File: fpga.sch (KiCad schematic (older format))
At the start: 1 part

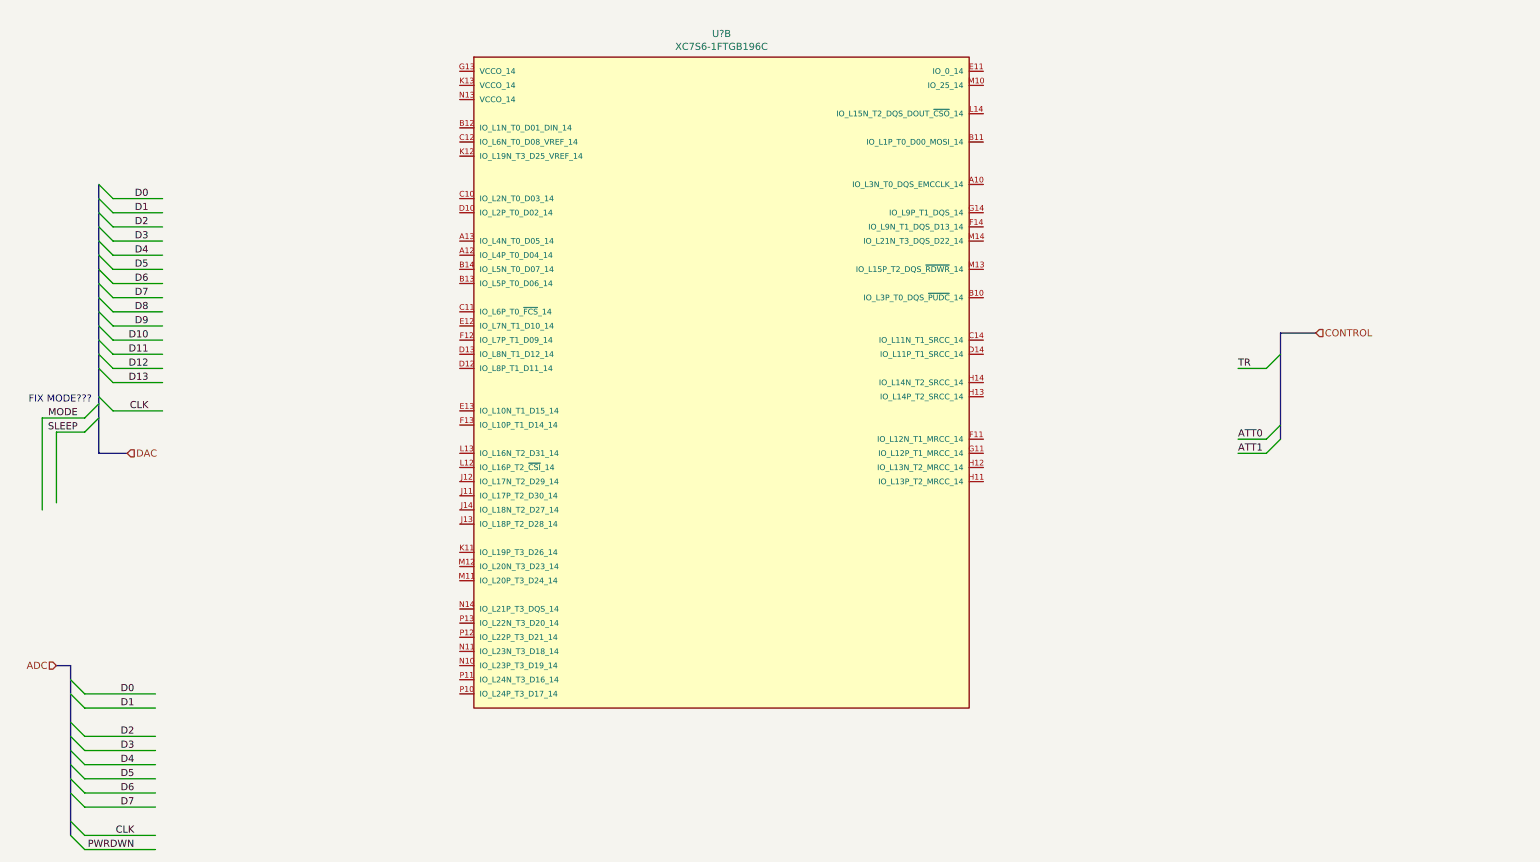
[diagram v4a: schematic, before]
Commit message: Begin the implementation of Human in-out, a few small changes
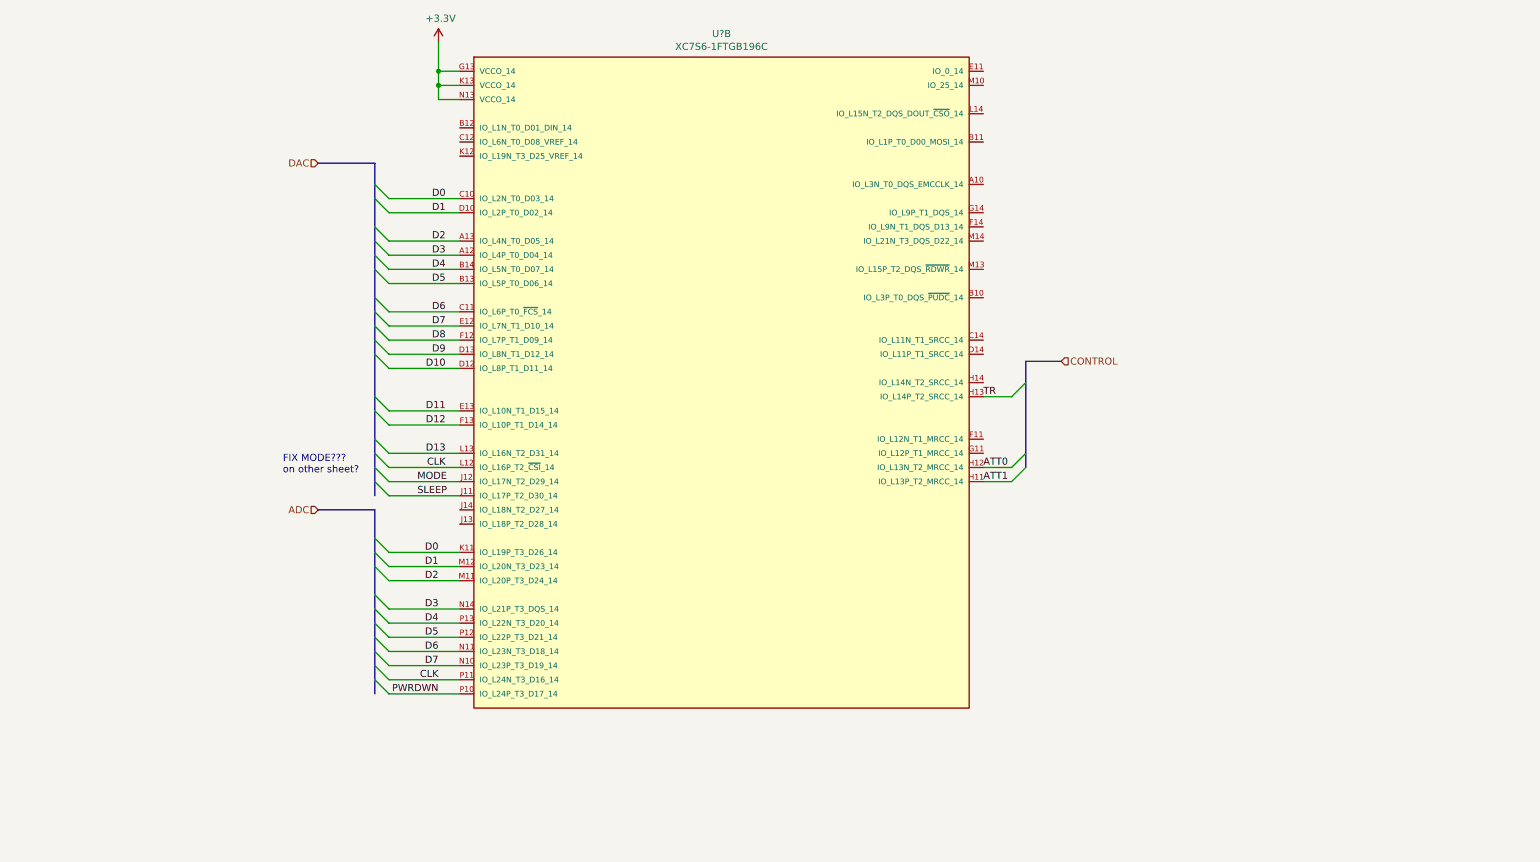
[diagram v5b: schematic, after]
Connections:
- net labels added: +3.3V
- wire segments 32 -> 36
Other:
- note added: "FIX MODE???\non other sheet?"
- note removed: "FIX MODE???"
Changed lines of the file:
@@
 $Descr A4 11693 8268
 encoding utf-8
-Sheet 11 16
+Sheet 11 17
 Title "Open HF SDR FPGA Sheet"
 Date "2021-01-16"
@@
 	1    0    0    -1
 $EndComp
-Text HLabel 1400 5800 0    50   Input ~ 0
+Text HLabel 3250 4700 0    50   Input ~ 0
 ADC
 Entry Wire Line
-	1500 5900 1600 6000
-Entry Wire Line
-	1600 6100 1500 6000
-Entry Wire Line
-	1600 6300 1500 6200
-Entry Wire Line
-	1600 6400 1500 6300
-Entry Wire Line
-	1600 6500 1500 6400
-Entry Wire Line
-	1600 6600 1500 6500
-Entry Wire Line
-	1600 6700 1500 6600
-Entry Wire Line
-	1600 6800 1500 6700
-Entry Wire Line
-	1600 7000 1500 6900
-Entry Wire Line
-	1600 7100 1500 7000
-Wire Wire Line
-	2100 6000 1600 6000
-Wire Wire Line
-	2100 6100 1600 6100
-Wire Wire Line
-	1600 6300 2100 6300
-Wire Wire Line
-	2100 6400 1600 6400
-Wire Wire Line
-	2100 6500 1600 6500
-Wire Wire Line
-	2100 6600 1600 6600
-Wire Wire Line
-	2100 6700 1600 6700
-Wire Wire Line
-	2100 6800 1600 6800
-Wire Wire Line
-	2100 7000 1600 7000
-Wire Wire Line
-	2100 7100 1600 7100
-Text Label 1950 6000 2    50   ~ 0
+	3650 4900 3750 5000
+Entry Wire Line
+	3750 5100 3650 5000
+Entry Wire Line
+	3750 5200 3650 5100
+Entry Wire Line
+	3750 5400 3650 5300
+Entry Wire Line
+	3750 5500 3650 5400
+Entry Wire Line
+	3750 5600 3650 5500
+Entry Wire Line
+	3750 5700 3650 5600
+Entry Wire Line
+	3750 5800 3650 5700
+Entry Wire Line
+	3750 5900 3650 5800
+Entry Wire Line
+	3750 6000 3650 5900
+Wire Wire Line
+	4250 5000 3750 5000
+Wire Wire Line
+	4250 5100 3750 5100
+Wire Wire Line
+	3750 5200 4250 5200
+Wire Wire Line
+	4250 5400 3750 5400
+Wire Wire Line
+	4250 5500 3750 5500
+Wire Wire Line
+	4250 5600 3750 5600
+Wire Wire Line
+	4250 5700 3750 5700
+Wire Wire Line
+	4250 5800 3750 5800
+Wire Wire Line
+	4250 5900 3750 5900
+Wire Wire Line
+	4250 6000 3750 6000
+Text Label 4100 5000 2    50   ~ 0
 D0
-Text Label 1950 6100 2    50   ~ 0
+Text Label 4100 5100 2    50   ~ 0
 D1
-Text Label 1950 6300 2    50   ~ 0
+Text Label 4100 5200 2    50   ~ 0
 D2
-Text Label 1950 6400 2    50   ~ 0
+Text Label 4100 5400 2    50   ~ 0
 D3
-Text Label 1950 6500 2    50   ~ 0
+Text Label 4100 5500 2    50   ~ 0
 D4
-Text Label 1950 6600 2    50   ~ 0
+Text Label 4100 5600 2    50   ~ 0
 D5
-Text Label 1950 6700 2    50   ~ 0
+Text Label 4100 5700 2    50   ~ 0
 D6
-Text Label 1950 6800 2    50   ~ 0
+Text Label 4100 5800 2    50   ~ 0
 D7
-Text Label 1950 7000 2    50   ~ 0
+Text Label 4100 5900 2    50   ~ 0
 CLK
-Text Label 1950 7100 2    50   ~ 0
+Text Label 4100 6000 2    50   ~ 0
 PWRDWN
-Wire Bus Line
-	1500 5800 1400 5800
-Entry Wire Line
-	1800 2500 1700 2400
-Entry Wire Line
-	1800 2600 1700 2500
-Entry Wire Line
-	1800 2700 1700 2600
-Entry Wire Line
-	1800 2800 1700 2700
-Entry Wire Line
-	1800 2900 1700 2800
-Entry Wire Line
-	1800 3000 1700 2900
-Entry Wire Line
-	1800 3100 1700 3000
-Entry Wire Line
-	1800 3200 1700 3100
-Entry Wire Line
-	1800 3300 1700 3200
-Entry Wire Line
-	1800 3400 1700 3300
-Entry Wire Line
-	1800 3500 1700 3400
-Entry Wire Line
-	1800 3600 1700 3500
-Entry Wire Line
-	1800 3700 1700 3600
-Entry Wire Line
-	1800 3800 1700 3700
-Entry Wire Line
-	1800 4000 1700 3900
-Wire Wire Line
-	2150 2500 1800 2500
-Wire Wire Line
-	2150 2600 1800 2600
-Wire Wire Line
-	2150 2700 1800 2700
-Wire Wire Line
-	2150 2800 1800 2800
-Wire Wire Line
-	2150 2900 1800 2900
-Wire Wire Line
-	2150 3000 1800 3000
-Wire Wire Line
-	2150 3100 1800 3100
-Wire Wire Line
-	2150 3200 1800 3200
-Wire Wire Line
-	2150 3300 1800 3300
-Wire Wire Line
-	2150 3400 1800 3400
-Wire Wire Line
-	2150 3500 1800 3500
-Wire Wire Line
-	2150 3600 1800 3600
-Wire Wire Line
-	2150 3700 1800 3700
-Wire Wire Line
-	2150 3800 1800 3800
-Wire Wire Line
-	2150 4000 1800 4000
-Text Label 2050 2500 2    50   ~ 0
+Entry Wire Line
+	3750 2500 3650 2400
+Entry Wire Line
+	3750 2600 3650 2500
+Entry Wire Line
+	3750 2800 3650 2700
+Entry Wire Line
+	3750 2900 3650 2800
+Entry Wire Line
+	3750 3000 3650 2900
+Entry Wire Line
+	3750 3100 3650 3000
+Entry Wire Line
+	3750 3300 3650 3200
+Entry Wire Line
+	3750 3400 3650 3300
+Entry Wire Line
+	3750 3500 3650 3400
+Entry Wire Line
+	3750 3600 3650 3500
+Entry Wire Line
+	3750 3700 3650 3600
+Entry Wire Line
+	3750 4000 3650 3900
+Entry Wire Line
+	3750 4100 3650 4000
+Entry Wire Line
+	3750 4300 3650 4200
+Entry Wire Line
+	3750 4400 3650 4300
+Wire Wire Line
+	4250 2500 3750 2500
+Wire Wire Line
+	4250 2600 3750 2600
+Wire Wire Line
+	4250 2800 3750 2800
+Wire Wire Line
+	4250 2900 3750 2900
+Wire Wire Line
+	4250 3000 3750 3000
+Wire Wire Line
+	4250 3100 3750 3100
+Wire Wire Line
+	4250 3300 3750 3300
+Wire Wire Line
+	4250 3400 3750 3400
+Wire Wire Line
+	4250 3500 3750 3500
+Wire Wire Line
+	4250 3600 3750 3600
+Wire Wire Line
+	4250 3700 3750 3700
+Wire Wire Line
+	4250 4000 3750 4000
+Wire Wire Line
+	4250 4100 3750 4100
+Wire Wire Line
+	4250 4300 3750 4300
+Wire Wire Line
+	4250 4400 3750 4400
+Text Label 4150 2500 2    50   ~ 0
 D0
-Text Label 2050 2600 2    50   ~ 0
+Text Label 4150 2600 2    50   ~ 0
 D1
-Text Label 2050 2700 2    50   ~ 0
+Text Label 4150 2800 2    50   ~ 0
 D2
-Text Label 2050 2800 2    50   ~ 0
+Text Label 4150 2900 2    50   ~ 0
 D3
-Text Label 2050 2900 2    50   ~ 0
+Text Label 4150 3000 2    50   ~ 0
 D4
-Text Label 2050 3000 2    50   ~ 0
+Text Label 4150 3100 2    50   ~ 0
 D5
-Text Label 2050 3100 2    50   ~ 0
+Text Label 4150 3300 2    50   ~ 0
 D6
-Text Label 2050 3200 2    50   ~ 0
+Text Label 4150 3400 2    50   ~ 0
 D7
-Text Label 2050 3300 2    50   ~ 0
+Text Label 4150 3500 2    50   ~ 0
 D8
-Text Label 2050 3400 2    50   ~ 0
+Text Label 4150 3600 2    50   ~ 0
 D9
-Text Label 2050 3500 2    50   ~ 0
+Text Label 4150 3700 2    50   ~ 0
 D10
-Text Label 2050 3600 2    50   ~ 0
+Text Label 4150 4000 2    50   ~ 0
 D11
-Text Label 2050 3700 2    50   ~ 0
+Text Label 4150 4100 2    50   ~ 0
 D12
-Text Label 2050 3800 2    50   ~ 0
+Text Label 4150 4300 2    50   ~ 0
 D13
-Text Label 2050 4000 2    50   ~ 0
+Text Label 4150 4400 2    50   ~ 0
 CLK
-Wire Bus Line
-	1700 4300 1900 4300
-Text HLabel 1900 4300 2    50   Input ~ 0
+Text HLabel 3250 2250 0    50   Input ~ 0
 DAC
-Wire Wire Line
-	1400 4650 1400 4150
-Entry Wire Line
-	1700 4050 1600 4150
-Wire Wire Line
-	1600 4150 1400 4150
-Text Label 1550 4150 2    50   ~ 0
+Entry Wire Line
+	3650 4500 3750 4600
+Text Label 3950 4600 0    50   ~ 0
 SLEEP
-Wire Wire Line
-	1300 4700 1300 4050
-Wire Wire Line
-	1300 4050 1600 4050
-Entry Wire Line
-	1700 3950 1600 4050
-Text Label 1550 4050 2    50   ~ 0
+Entry Wire Line
+	3650 4400 3750 4500
+Text Label 3950 4500 0    50   ~ 0
 MODE
-Text Notes 1650 3950 2    50   ~ 0
-FIX MODE???
-Text Label 9750 4200 0    50   ~ 0
+Text Notes 3000 4450 0    50   ~ 0
+FIX MODE???\non other sheet?
+Text Label 7950 4400 0    50   ~ 0
 ATT0
-Text Label 9750 4300 0    50   ~ 0
+Text Label 7950 4500 0    50   ~ 0
 ATT1
-Text Label 9750 3700 0    50   ~ 0
+Text Label 7950 3900 0    50   ~ 0
 TR
 Wire Bus Line
-	10050 3450 10300 3450
-Text HLabel 10300 3450 2    50   Input ~ 0
+	8250 3650 8500 3650
+Text HLabel 8500 3650 2    50   Input ~ 0
 CONTROL
 Entry Wire Line
-	9950 3700 10050 3600
-Entry Wire Line
-	9950 4300 10050 4200
-Entry Wire Line
-	9950 4200 10050 4100
-Wire Wire Line
-	9950 4200 9750 4200
-Wire Wire Line
-	9750 4300 9950 4300
-Wire Wire Line
-	9950 3700 9750 3700
-Wire Bus Line
-	10050 3450 10050 4200
-Wire Bus Line
-	1500 5800 1500 7000
-Wire Bus Line
-	1700 2400 1700 4300
+	8150 3900 8250 3800
+Entry Wire Line
+	8150 4500 8250 4400
+Entry Wire Line
+	8150 4400 8250 4300
+Wire Wire Line
+	8150 4400 7950 4400
+Wire Wire Line
+	7950 4500 8150 4500
+Wire Wire Line
+	8150 3900 7950 3900
+Wire Wire Line
+	3750 4600 4250 4600
+Wire Wire Line
+	3750 4500 4250 4500
+Wire Bus Line
+	3250 2250 3650 2250
+Wire Bus Line
+	3250 4700 3650 4700
+$Comp
+L power:+3.3V #PWR?
+U 1 1 60904776
+P 4100 1400
+F 0 "#PWR?" H 4100 1250 50  0001 C CNN
+F 1 "+3.3V" H 4115 1573 50  0000 C CNN
+F 2 "" H 4100 1400 50  0001 C CNN
+F 3 "" H 4100 1400 50  0001 C CNN
+	1    4100 1400
+	1    0    0    -1
+$EndComp
+Wire Wire Line
+	4250 1800 4100 1800
+Wire Wire Line
+	4100 1800 4100 1700
+Wire Wire Line
+	4250 1600 4100 1600
+Connection ~ 4100 1600
+Wire Wire Line
+	4100 1600 4100 1400
+Wire Wire Line
+	4250 1700 4100 1700
+Wire Bus Line
+	8250 3650 8250 4400
+Wire Bus Line
+	3650 4700 3650 6000
+Wire Bus Line
+	3650 2250 3650 4600
+Connection ~ 4100 1700
+Wire Wire Line
+	4100 1700 4100 1600
 $EndSCHEMATC

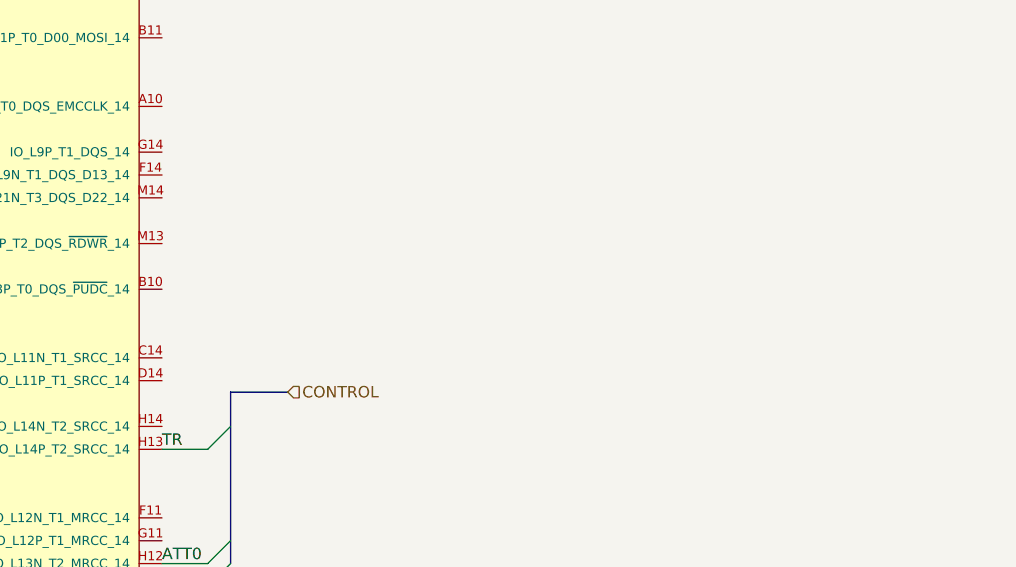
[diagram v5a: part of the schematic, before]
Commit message: Progress in programmer sheet
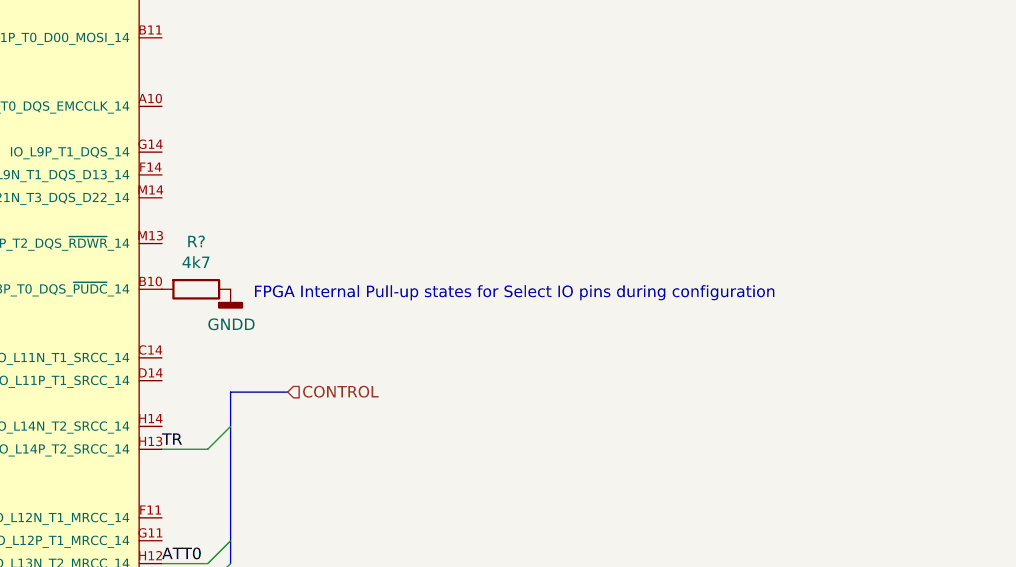
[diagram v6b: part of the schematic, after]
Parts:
- added R?: 4k7, symbol Device:R
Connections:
- net at U?.B10 (IO_L3P_T0_DQS_~PUDC~_14): now also R?.2
- new net GNDD: R?.1
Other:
- note added: "FPGA Internal Pull-up states for Select IO pins during configuration"
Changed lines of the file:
@@
 U 1 1 60904776
 P 4100 1400
+AR Path="/60904776" Ref="#PWR?"  Part="1"
+AR Path="/6004B243/60904776" Ref="#PWR?"  Part="1"
 F 0 "#PWR?" H 4100 1250 50  0001 C CNN
 F 1 "+3.3V" H 4115 1573 50  0000 C CNN
@@
 Wire Wire Line
 	4250 1700 4100 1700
+Connection ~ 4100 1700
+Wire Wire Line
+	4100 1700 4100 1600
 Wire Bus Line
 	8250 3650 8250 4400
@@
 Wire Bus Line
 	3650 2250 3650 4600
-Connection ~ 4100 1700
-Wire Wire Line
-	4100 1700 4100 1600
+$Comp
+L Device:R R?
+U 1 1 609B728D
+P 8100 3200
+F 0 "R?" V 7893 3200 50  0000 C CNN
+F 1 "4k7" V 7984 3200 50  0000 C CNN
+F 2 "" V 8030 3200 50  0001 C CNN
+F 3 "~" H 8100 3200 50  0001 C CNN
+	1    8100 3200
+	0    1    1    0
+$EndComp
+$Comp
+L power:GNDD #PWR?
+U 1 1 609B7D59
+P 8250 3200
+F 0 "#PWR?" H 8250 2950 50  0001 C CNN
+F 1 "GNDD" H 8254 3045 50  0000 C CNN
+F 2 "" H 8250 3200 50  0001 C CNN
+F 3 "" H 8250 3200 50  0001 C CNN
+	1    8250 3200
+	1    0    0    -1
+$EndComp
+Text Notes 8350 3250 0    50   ~ 0
+FPGA Internal Pull-up states for Select IO pins during configuration
 $EndSCHEMATC
